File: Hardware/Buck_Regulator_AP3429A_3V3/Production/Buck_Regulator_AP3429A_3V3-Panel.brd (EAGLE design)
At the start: 226.8 x 169.2 mm, 2502 parts, among them J1 Screw Terminal, J10 Breakout Headers, J100 Breakout Headers, J101 Screw Terminal, J102 POWER_JACKPOWER_JACK_SLOT_COM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, J103 Breakout Headers, J104 Screw Terminal, J105 POWER_JACKPOWER_JACK_SLOT_COM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, J106 Breakout Headers, J107 Screw Terminal, J108 POWER_JACKPOWER_JACK_SLOT_COM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, J109 Breakout Headers, J11 Screw Terminal, J110 Screw Terminal, J111 POWER_JACKPOWER_JACK_SLOT_COM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, J112 Breakout Headers, J113 Screw Terminal, J114 POWER_JACKPOWER_JACK_SLOT_COM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, J115 Breakout Headers, J116 Screw Terminal, J117 POWER_JACKPOWER_JACK_SLOT_COM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, J118 Breakout Headers, J119 Screw Terminal, J12 POWER_JACKPOWER_JACK_SLOT_COM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, J120 POWER_JACKPOWER_JACK_SLOT_COM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, J121 Breakout Headers, J122 Screw Terminal, J123 POWER_JACKPOWER_JACK_SLOT_COM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, J124 Breakout Headers, J125 Screw Terminal, J126 POWER_JACKPOWER_JACK_SLOT_COM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, J127 Breakout Headers, J128 Screw Terminal, J129 POWER_JACKPOWER_JACK_SLOT_COM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, J13 Breakout Headers, J130 Breakout Headers, J131 Screw Terminal, J132 POWER_JACKPOWER_JACK_SLOT_COM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, J133 Breakout Headers, J134 Screw Terminal, J135 POWER_JACKPOWER_JACK_SLOT_COM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, J136 Breakout Headers, J137 Screw Terminal, J138 POWER_JACKPOWER_JACK_SLOT_COM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, J139 Breakout Headers, J14 Screw Terminal, J140 Screw Terminal, J141 POWER_JACKPOWER_JACK_SLOT_COM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, J142 Breakout Headers, J143 Screw Terminal, J144 POWER_JACKPOWER_JACK_SLOT_COM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, J15 POWER_JACKPOWER_JACK_SLOT_COM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, J16 Breakout Headers, J17 Screw Terminal, J18 POWER_JACKPOWER_JACK_SLOT_COM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, J19 Breakout Headers, J2 POWER_JACKPOWER_JACK_SLOT_COM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, J20 Screw Terminal, J21 POWER_JACKPOWER_JACK_SLOT_COM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, J22 Breakout Headers, J23 Screw Terminal, J24 POWER_JACKPOWER_JACK_SLOT_COM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, J25 Breakout Headers, J26 Screw Terminal, J27 POWER_JACKPOWER_JACK_SLOT_COM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, J28 Breakout Headers, J29 Screw Terminal, J3 Breakout Headers, J30 POWER_JACKPOWER_JACK_SLOT_COM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, J31 Breakout Headers, J32 Screw Terminal, J33 POWER_JACKPOWER_JACK_SLOT_COM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, J34 Breakout Headers, J35 Screw Terminal, J36 POWER_JACKPOWER_JACK_SLOT_COM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, J37 Breakout Headers, J38 Screw Terminal, J39 POWER_JACKPOWER_JACK_SLOT_COM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, J4 Breakout Headers, J40 Breakout Headers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

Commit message: Updated panelized files
Adjusted via to no longer be in the way of the bStop on the back for the thermal pad on the backside. Included ordering instructions on the brd files for both 1.8V and 3.3V
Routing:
- net N$59: track 36.4 -> 36.9 mm
- net N$27: track 36.4 -> 36.9 mm
- net N$91: track 36.4 -> 36.9 mm
- net N$187: track 36.4 -> 36.9 mm
- net N$155: track 36.4 -> 36.9 mm
- net N$123: track 36.4 -> 36.9 mm
- net N$99: track 36.4 -> 36.9 mm
- net N$75: track 36.4 -> 36.9 mm
- net N$71: track 36.4 -> 36.9 mm
- net N$7: track 36.4 -> 36.9 mm
- net N$67: track 36.4 -> 36.9 mm
- net N$47: track 36.4 -> 36.9 mm
- net N$43: track 36.4 -> 36.9 mm
- net N$39: track 36.4 -> 36.9 mm
- net N$35: track 36.4 -> 36.9 mm
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
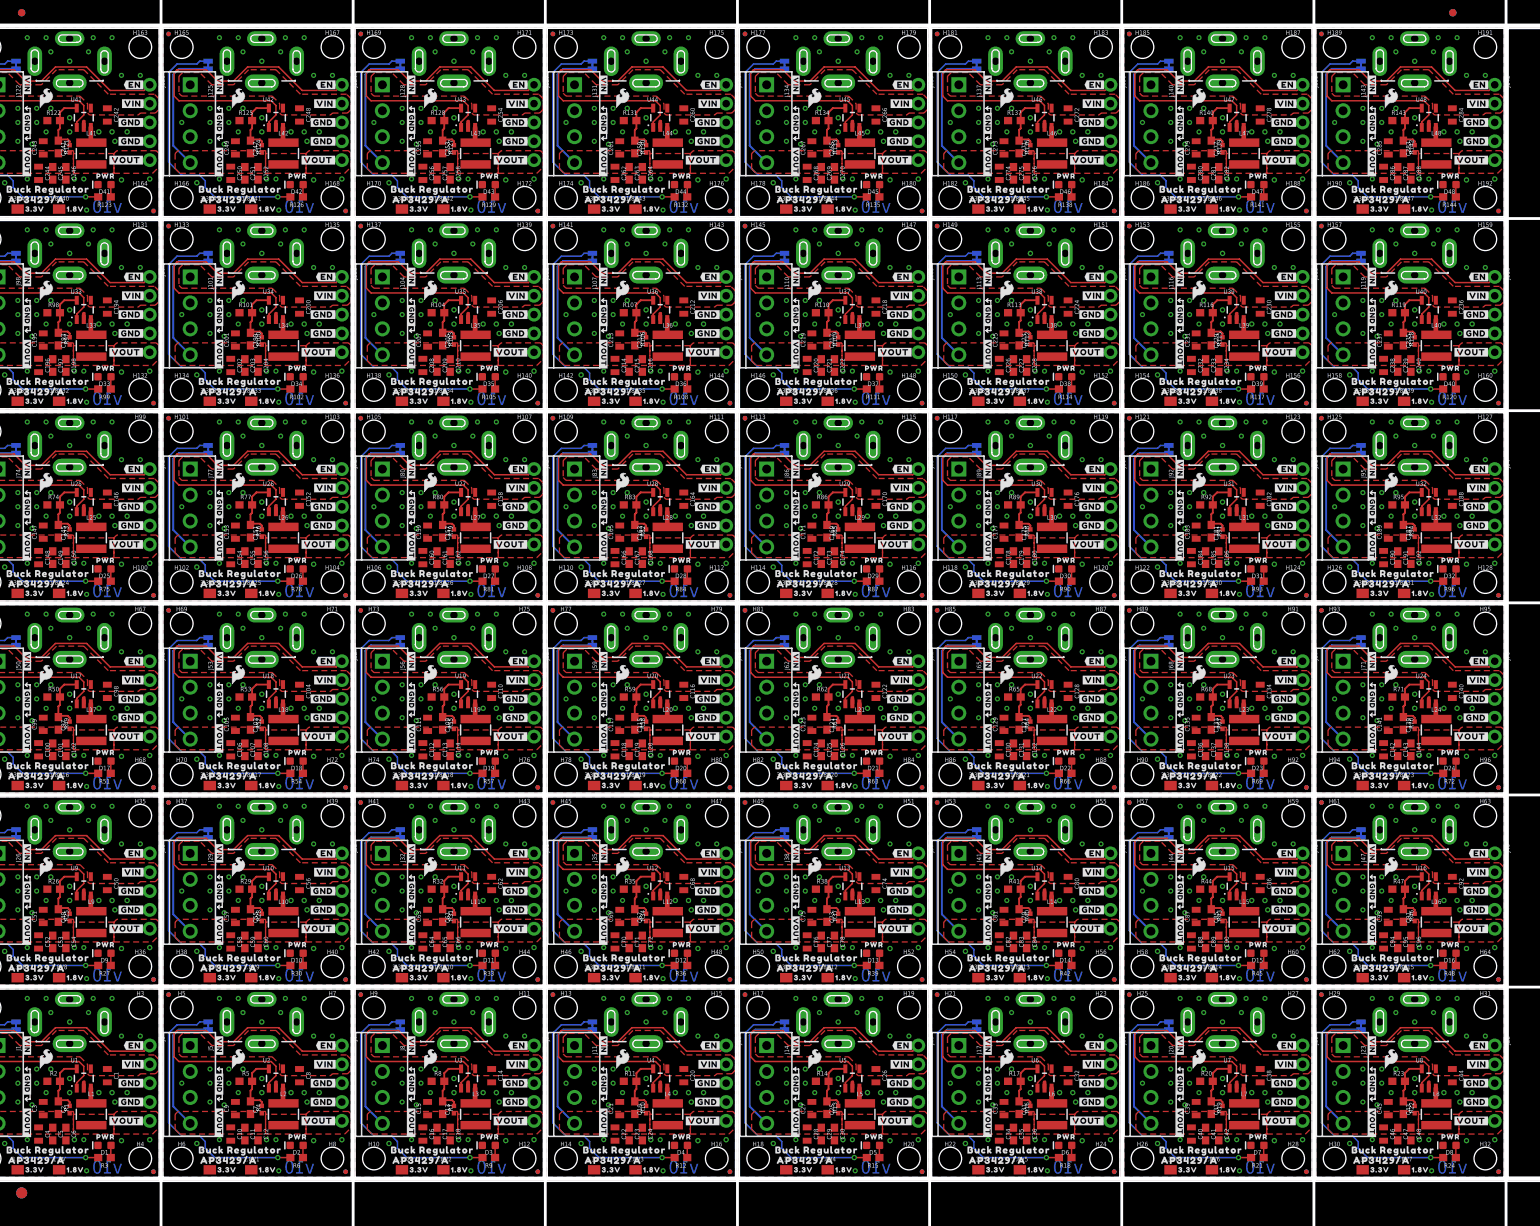
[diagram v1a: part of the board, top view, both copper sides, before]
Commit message: V11 Design Update
Added 100k resistor to pull EN high to VIN for an easier plug and play application.
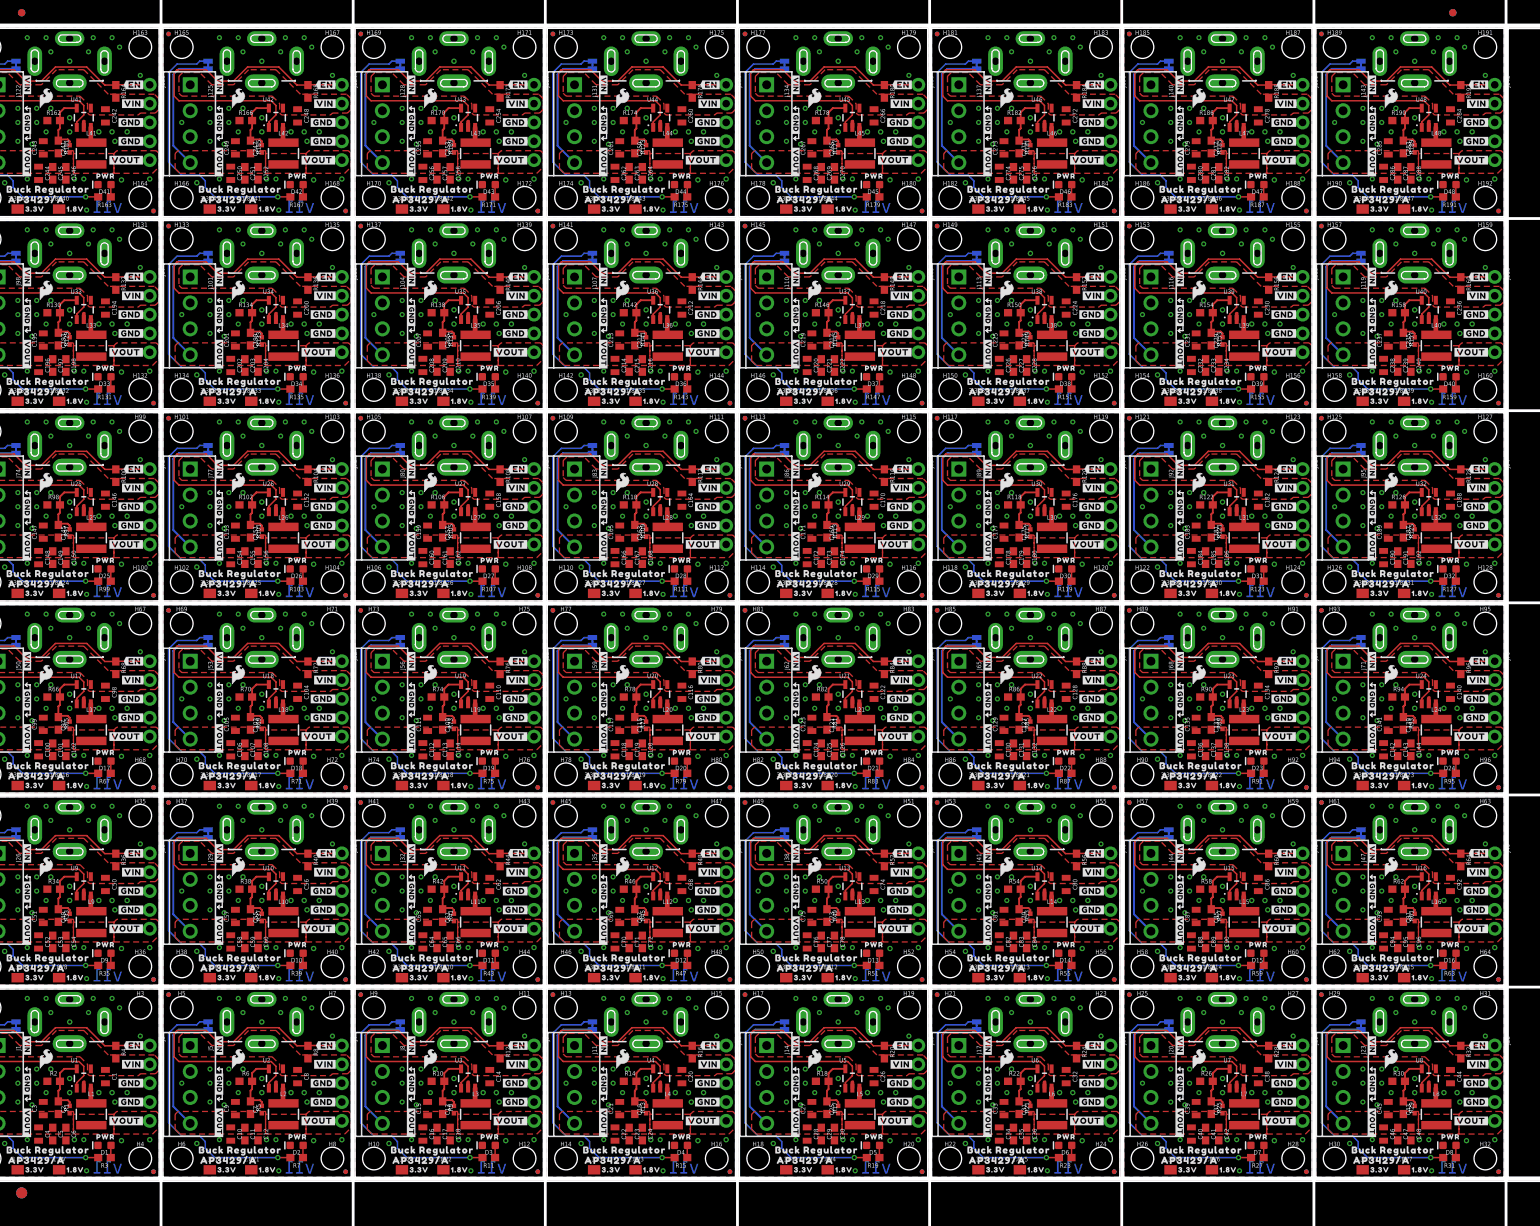
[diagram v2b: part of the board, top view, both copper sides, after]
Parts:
- added R145, R149, R153, R157, R161, R165, R169, R173, R177, R181, R185, R189: 453k, SparkFun-Resistors:0603
- added R146, R148, R150, R152, R154, R156, R158, R160, R162, R164, R166, R168, R170, R172, R174, R176, R178, R180, R182, R184, R186, R188, R190, R192: 100k, SparkFun-Resistors:0603
- added R147, R151, R155, R159, R163, R167, R171, R175, R179, R183, R187, R191: 1k, SparkFun-Resistors:0603
- R10, R100, R106, R112, R118, R124, R130, R136, R142, R16, R22, R28, R34, R4, R40, R46, R52, R58, R64, R70, R76, R82, R88, R94: value 453k -> 100k
- R101, R113, R125, R137, R17, R29, R41, R5, R53, R65, R77, R89: value 100k -> 453k
- R102, R108, R114, R12, R120, R126, R132, R138, R144, R18, R24, R30, R36, R42, R48, R54, R6, R60, R66, R72, R78, R84, R90, R96: value 1k -> 100k
- R103, R115, R127, R139, R19, R31, R43, R55, R67, R7, R79, R91: value 453k -> 1k
- R105, R117, R129, R141, R21, R33, R45, R57, R69, R81, R9, R93: value 1k -> 453k
- R107, R11, R119, R131, R143, R23, R35, R47, R59, R71, R83, R95: value 100k -> 1k
- moved R125 165.6 mm to (193.2, 87.1), turned to 270 degrees
- moved R122 163.9 mm to (166.6, 90.7)
- moved R123 163.9 mm to (173.5, 80.4)
- moved R121 163.9 mm to (167.3, 87.1)
- moved R29 158.8 mm to (193.2, 9.40), turned to 270 degrees
- moved R26 157.6 mm to (166.6, 13.0)
- moved R27 157.6 mm to (173.5, 2.67)
- moved R25 157.6 mm to (167.3, 9.40)
- moved R70 156.1 mm to (37.1, 64.8), turned to 0 degrees
- moved R72 154.6 mm to (45.5, 68.7), turned to 270 degrees
- moved R126 154.3 mm to (192.5, 90.7), turned to 0 degrees
- moved R30 149.4 mm to (192.5, 13.0), turned to 0 degrees
- moved R67 149.4 mm to (18.0, 54.5), turned to 180 degrees
- moved R71 148.9 mm to (43.9, 54.5), turned to 180 degrees
- moved R127 147.8 mm to (199.4, 80.4), turned to 180 degrees
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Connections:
- net EN: now also R4.1
- net EN1: now also R8.1
- net EN10: now also R44.1
- net EN11: now also R48.1
- net EN12: now also R52.1
- net EN13: now also R56.1
- net EN14: now also R60.1
- net EN15: now also R64.1
- net EN16: now also R68.1
- net EN17: now also R72.1
- net EN18: now also R76.1
- net EN19: now also R80.1
- net EN2: now also R12.1
- net EN20: now also R84.1
- net EN21: now also R88.1
- net EN22: now also R92.1
- net EN23: now also R96.1
- net EN24: now also R100.1
- net EN25: now also R104.1
- net EN26: now also R108.1
- net EN27: now also R112.1
- net EN28: now also R116.1
- net EN29: now also R120.1
- net EN3: now also R16.1
- net EN30: now also R124.1
- net EN31: now also R128.1
- net EN32: now also R132.1
- net EN33: now also R136.1
- net EN34: now also R140.1
- net EN35: now also R144.1
- net EN36: now also R148.1
- net EN37: now also R152.1
- net EN38: now also R156.1
- net EN39: now also R160.1
- net EN4: now also R20.1
- net EN40: now also R164.1
- net EN41: now also R168.1
- net EN42: now also R172.1
- net EN43: now also R176.1
- net EN44: now also R180.1
- net EN45: now also R184.1
- net EN46: now also R188.1
- net EN47: now also R192.1
- net EN5: now also R24.1
- net EN6: now also R28.1
- net EN7: now also R32.1
- net EN8: now also R36.1
- net EN9: now also R40.1
- net GND1: now also R6.1; no longer R5.1
- net GND10: now also R42.1; no longer R32.1
- net GND11: now also R46.1; no longer R35.1
- net GND12: now also R50.1; no longer R38.1
- net GND13: now also R54.1; no longer R41.1
- net GND14: now also R58.1; no longer R44.1
- net GND15: now also R62.1; no longer R47.1
- net GND16: now also R66.1; no longer R50.1
- net GND17: now also R70.1; no longer R53.1
- net GND18: now also R74.1; no longer R56.1
- net GND19: now also R78.1; no longer R59.1
- net GND2: now also R10.1; no longer R8.1
- net GND20: now also R82.1; no longer R62.1
- net GND21: now also R86.1; no longer R65.1
- net GND22: now also R90.1; no longer R68.1
- net GND23: now also R94.1; no longer R71.1
- net GND24: now also R98.1; no longer R74.1
- net GND25: now also R102.1; no longer R77.1
- net GND26: now also R106.1; no longer R80.1
- net GND27: now also R110.1; no longer R83.1
- net GND28: now also R114.1; no longer R86.1
- net GND29: now also R118.1; no longer R89.1
- net GND3: now also R14.1; no longer R11.1
- net GND30: now also R122.1; no longer R92.1
- net GND31: now also R126.1; no longer R95.1
- net GND32: now also R130.1; no longer R98.1
- net GND33: now also R134.1; no longer R101.1
- net GND34: now also R138.1; no longer R104.1
- net GND35: now also R142.1; no longer R107.1
- net GND36: now also R146.1; no longer R110.1
- net GND37: now also R150.1; no longer R113.1
- net GND38: now also R154.1; no longer R116.1
- net GND39: now also R158.1; no longer R119.1
- net GND4: now also R18.1; no longer R14.1
- net GND40: now also R162.1; no longer R122.1
- net GND41: now also R166.1; no longer R125.1
- net GND42: now also R170.1; no longer R128.1
- net GND43: now also R174.1; no longer R131.1
- net GND44: now also R178.1; no longer R134.1
- net GND45: now also R182.1; no longer R137.1
- net GND46: now also R186.1; no longer R140.1
- net GND47: now also R190.1; no longer R143.1
- net GND5: now also R22.1; no longer R17.1
- net GND6: now also R26.1; no longer R20.1
- net GND7: now also R30.1; no longer R23.1
- net GND8: now also R34.1; no longer R26.1
- net GND9: now also R38.1; no longer R29.1
- net N$10: now also R10.2, R9.1; no longer R7.1, R8.2
- net N$100: now also R99.1; no longer R75.1
- net N$102: now also R101.1, R102.2; no longer R76.1, R77.2
- net N$103: now also R103.2; no longer R78.2
- net N$104: now also R103.1; no longer R78.1
- net N$106: now also R105.1, R106.2; no longer R79.1, R80.2
- net N$107: now also R107.2; no longer R81.2
- net N$108: now also R107.1; no longer R81.1
- net N$11: now also R11.2; no longer R9.2
- net N$110: now also R109.1, R110.2; no longer R82.1, R83.2
- net N$111: now also R111.2; no longer R84.2
- net N$112: now also R111.1; no longer R84.1
- net N$114: now also R113.1, R114.2; no longer R85.1, R86.2
- net N$115: now also R115.2; no longer R87.2
- net N$116: now also R115.1; no longer R87.1
- net N$118: now also R117.1, R118.2; no longer R88.1, R89.2
- net N$119: now also R119.2; no longer R90.2
- net N$12: now also R11.1; no longer R9.1
- net N$120: now also R119.1; no longer R90.1
- net N$122: now also R121.1, R122.2; no longer R91.1, R92.2
- net N$123: now also R123.2; no longer R93.2
- net N$124: now also R123.1; no longer R93.1
- net N$126: now also R125.1, R126.2; no longer R94.1, R95.2
- net N$127: now also R127.2; no longer R96.2
- net N$128: now also R127.1; no longer R96.1
- net N$130: now also R129.1, R130.2; no longer R97.1, R98.2
- net N$131: now also R131.2; no longer R99.2
- net N$132: now also R131.1; no longer R99.1
- net N$134: now also R133.1, R134.2; no longer R100.1, R101.2
- net N$135: now also R135.2; no longer R102.2
- net N$136: now also R135.1; no longer R102.1
- net N$138: now also R137.1, R138.2; no longer R103.1, R104.2
- net N$139: now also R139.2; no longer R105.2
- net N$14: now also R13.1, R14.2; no longer R10.1, R11.2
- net N$140: now also R139.1; no longer R105.1
- net N$142: now also R141.1, R142.2; no longer R106.1, R107.2
- net N$143: now also R143.2; no longer R108.2
- net N$144: now also R143.1; no longer R108.1
- net N$146: now also R145.1, R146.2; no longer R109.1, R110.2
- net N$147: now also R147.2; no longer R111.2
- net N$148: now also R147.1; no longer R111.1
- net N$15: now also R15.2; no longer R12.2
- net N$150: now also R149.1, R150.2; no longer R112.1, R113.2
- net N$151: now also R151.2; no longer R114.2
- net N$152: now also R151.1; no longer R114.1
- net N$154: now also R153.1, R154.2; no longer R115.1, R116.2
- net N$155: now also R155.2; no longer R117.2
- net N$156: now also R155.1; no longer R117.1
- net N$158: now also R157.1, R158.2; no longer R118.1, R119.2
- net N$159: now also R159.2; no longer R120.2
- net N$16: now also R15.1; no longer R12.1
- net N$160: now also R159.1; no longer R120.1
- net N$162: now also R161.1, R162.2; no longer R121.1, R122.2
- net N$163: now also R163.2; no longer R123.2
- net N$164: now also R163.1; no longer R123.1
- net N$166: now also R165.1, R166.2; no longer R124.1, R125.2
- net N$167: now also R167.2; no longer R126.2
- net N$168: now also R167.1; no longer R126.1
- net N$170: now also R169.1, R170.2; no longer R127.1, R128.2
- net N$171: now also R171.2; no longer R129.2
- net N$172: now also R171.1; no longer R129.1
- net N$174: now also R173.1, R174.2; no longer R130.1, R131.2
- net N$175: now also R175.2; no longer R132.2
- net N$176: now also R175.1; no longer R132.1
- net N$178: now also R177.1, R178.2; no longer R133.1, R134.2
- net N$179: now also R179.2; no longer R135.2
- net N$18: now also R17.1, R18.2; no longer R13.1, R14.2
- net N$180: now also R179.1; no longer R135.1
- net N$182: now also R181.1, R182.2; no longer R136.1, R137.2
- net N$183: now also R183.2; no longer R138.2
- net N$184: now also R183.1; no longer R138.1
- net N$186: now also R185.1, R186.2; no longer R139.1, R140.2
- net N$187: now also R187.2; no longer R141.2
- net N$188: now also R187.1; no longer R141.1
- net N$19: now also R19.2; no longer R15.2
- net N$190: now also R189.1, R190.2; no longer R142.1, R143.2
- net N$191: now also R191.2; no longer R144.2
- net N$192: now also R191.1; no longer R144.1
- net N$20: now also R19.1; no longer R15.1
- net N$22: now also R21.1, R22.2; no longer R16.1, R17.2
- net N$23: now also R23.2; no longer R18.2
- net N$24: now also R23.1; no longer R18.1
- net N$26: now also R25.1, R26.2; no longer R19.1, R20.2
- net N$27: now also R27.2; no longer R21.2
- net N$28: now also R27.1; no longer R21.1
- net N$30: now also R29.1, R30.2; no longer R22.1, R23.2
- net N$31: now also R31.2; no longer R24.2
- net N$32: now also R31.1; no longer R24.1
- net N$34: now also R33.1, R34.2; no longer R25.1, R26.2
- net N$35: now also R35.2; no longer R27.2
- net N$36: now also R35.1; no longer R27.1
- net N$38: now also R37.1, R38.2; no longer R28.1, R29.2
- net N$39: now also R39.2; no longer R30.2
- net N$40: now also R39.1; no longer R30.1
- net N$42: now also R41.1, R42.2; no longer R31.1, R32.2
- net N$43: now also R43.2; no longer R33.2
- net N$44: now also R43.1; no longer R33.1
- net N$46: now also R45.1, R46.2; no longer R34.1, R35.2
- net N$47: now also R47.2; no longer R36.2
- net N$48: now also R47.1; no longer R36.1
- net N$50: now also R49.1, R50.2; no longer R37.1, R38.2
- net N$51: now also R51.2; no longer R39.2
- net N$52: now also R51.1; no longer R39.1
- net N$54: now also R53.1, R54.2; no longer R40.1, R41.2
- net N$55: now also R55.2; no longer R42.2
- net N$56: now also R55.1; no longer R42.1
- net N$58: now also R57.1, R58.2; no longer R43.1, R44.2
- net N$59: now also R59.2; no longer R45.2
- net N$6: now also R5.1, R6.2; no longer R4.1, R5.2
- net N$60: now also R59.1; no longer R45.1
- net N$62: now also R61.1, R62.2; no longer R46.1, R47.2
- net N$63: now also R63.2; no longer R48.2
- net N$64: now also R63.1; no longer R48.1
- net N$66: now also R65.1, R66.2; no longer R49.1, R50.2
- net N$67: now also R67.2; no longer R51.2
- net N$68: now also R67.1; no longer R51.1
- net N$7: now also R7.2; no longer R6.2
- net N$70: now also R69.1, R70.2; no longer R52.1, R53.2
- net N$71: now also R71.2; no longer R54.2
- net N$72: now also R71.1; no longer R54.1
- net N$74: now also R73.1, R74.2; no longer R55.1, R56.2
- net N$75: now also R75.2; no longer R57.2
- net N$76: now also R75.1; no longer R57.1
- net N$78: now also R77.1, R78.2; no longer R58.1, R59.2
- net N$79: now also R79.2; no longer R60.2
- net N$8: now also R7.1; no longer R6.1
- net N$80: now also R79.1; no longer R60.1
- net N$82: now also R81.1, R82.2; no longer R61.1, R62.2
- net N$83: now also R83.2; no longer R63.2
- net N$84: now also R83.1; no longer R63.1
- net N$86: now also R85.1, R86.2; no longer R64.1, R65.2
- net N$87: now also R87.2; no longer R66.2
- net N$88: now also R87.1; no longer R66.1
- net N$90: now also R89.1, R90.2; no longer R67.1, R68.2
- net N$91: now also R91.2; no longer R69.2
- net N$92: now also R91.1; no longer R69.1
- net N$94: now also R93.1, R94.2; no longer R70.1, R71.2
- net N$95: now also R95.2; no longer R72.2
- net N$96: now also R95.1; no longer R72.1
- net N$98: now also R97.1, R98.2; no longer R73.1, R74.2
- net N$99: now also R99.2; no longer R75.2
- net VIN: now also R4.2
- net VIN1: now also R8.2
- net VIN10: now also R44.2
- net VIN11: now also R48.2
- net VIN12: now also R52.2
- net VIN13: now also R56.2
- net VIN14: now also R60.2
- net VIN15: now also R64.2
- net VIN16: now also R68.2
- net VIN17: now also R72.2
- net VIN18: now also R76.2
- net VIN19: now also R80.2
- net VIN2: now also R12.2
- net VIN20: now also R84.2
- net VIN21: now also R88.2
- net VIN22: now also R92.2
- net VIN23: now also R96.2
- net VIN24: now also R100.2
- net VIN25: now also R104.2
- net VIN26: now also R108.2
- net VIN27: now also R112.2
- net VIN28: now also R116.2
- net VIN29: now also R120.2
- net VIN3: now also R16.2
- net VIN30: now also R124.2
- net VIN31: now also R128.2
- net VIN32: now also R132.2
- net VIN33: now also R136.2
- net VIN34: now also R140.2
- net VIN35: now also R144.2
- net VIN36: now also R148.2
- net VIN37: now also R152.2
- net VIN38: now also R156.2
- net VIN39: now also R160.2
- net VIN4: now also R20.2
- net VIN40: now also R164.2
- net VIN41: now also R168.2
- net VIN42: now also R172.2
- net VIN43: now also R176.2
- net VIN44: now also R180.2
- net VIN45: now also R184.2
- net VIN46: now also R188.2
- net VIN47: now also R192.2
- net VIN5: now also R24.2
- net VIN6: now also R28.2
- net VIN7: now also R32.2
- net VIN8: now also R36.2
- net VIN9: now also R40.2
- net VOUT1: now also R5.2; no longer R4.2
- net VOUT10: now also R41.2; no longer R31.2
- net VOUT11: now also R45.2; no longer R34.2
- net VOUT12: now also R49.2; no longer R37.2
- net VOUT13: now also R53.2; no longer R40.2
- net VOUT14: now also R57.2; no longer R43.2
- net VOUT15: now also R61.2; no longer R46.2
- net VOUT16: now also R65.2; no longer R49.2
- net VOUT17: now also R69.2; no longer R52.2
- net VOUT18: now also R73.2; no longer R55.2
- net VOUT19: now also R77.2; no longer R58.2
- net VOUT2: now also R9.2; no longer R7.2
- net VOUT20: now also R81.2; no longer R61.2
- net VOUT21: now also R85.2; no longer R64.2
- net VOUT22: now also R89.2; no longer R67.2
- net VOUT23: now also R93.2; no longer R70.2
- net VOUT24: now also R97.2; no longer R73.2
- net VOUT25: now also R101.2; no longer R76.2
- net VOUT26: now also R105.2; no longer R79.2
- net VOUT27: now also R109.2; no longer R82.2
- net VOUT28: now also R113.2; no longer R85.2
- net VOUT29: now also R117.2; no longer R88.2
- net VOUT3: now also R13.2; no longer R10.2
- net VOUT30: now also R121.2; no longer R91.2
- net VOUT31: now also R125.2; no longer R94.2
- net VOUT32: now also R129.2; no longer R97.2
- net VOUT33: now also R133.2; no longer R100.2
- net VOUT34: now also R137.2; no longer R103.2
- net VOUT35: now also R141.2; no longer R106.2
- net VOUT36: now also R145.2; no longer R109.2
- net VOUT37: now also R149.2; no longer R112.2
- net VOUT38: now also R153.2; no longer R115.2
- net VOUT39: now also R157.2; no longer R118.2
- net VOUT4: now also R17.2; no longer R13.2
- net VOUT40: now also R161.2; no longer R121.2
- net VOUT41: now also R165.2; no longer R124.2
- net VOUT42: now also R169.2; no longer R127.2
- net VOUT43: now also R173.2; no longer R130.2
- net VOUT44: now also R177.2; no longer R133.2
- net VOUT45: now also R181.2; no longer R136.2
- net VOUT46: now also R185.2; no longer R139.2
- net VOUT47: now also R189.2; no longer R142.2
- net VOUT5: now also R21.2; no longer R16.2
- net VOUT6: now also R25.2; no longer R19.2
- net VOUT7: now also R29.2; no longer R22.2
- net VOUT8: now also R33.2; no longer R25.2
- net VOUT9: now also R37.2; no longer R28.2
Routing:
- net EN40: track 46.6 -> 46.0 mm
- net EN46: track 46.6 -> 46.0 mm
- net EN45: track 46.6 -> 46.0 mm
- net EN41: track 46.6 -> 46.0 mm
- net EN47: track 46.6 -> 46.0 mm
- net EN44: track 46.6 -> 46.0 mm
- net EN43: track 46.6 -> 46.0 mm
- net EN42: track 46.6 -> 46.0 mm
- net EN9: track 46.6 -> 46.0 mm
- net EN7: track 46.6 -> 46.0 mm
- net EN4: track 46.6 -> 46.0 mm
- net EN39: track 46.6 -> 46.0 mm
- net EN3: track 46.6 -> 46.0 mm
- net EN2: track 46.6 -> 46.0 mm
- net EN17: track 46.6 -> 46.0 mm
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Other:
- board text added: "v11"
- board text removed: "v10"
